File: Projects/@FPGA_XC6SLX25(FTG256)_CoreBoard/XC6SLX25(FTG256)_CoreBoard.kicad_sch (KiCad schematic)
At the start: 155 parts, among them J1 MTA18ASF2G72HZ-2G3A2, U1 XC6SLX25-FTG256, U2 W25Q128JVS, U3 TPS51200DRC, U4 MP214x, U5 MP214x, U6 MP214x, U7 MP214x, X1 ECS-2520MV-xxx-xx

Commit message: XC6SLX25(FTG256)_CoreBoard Checked
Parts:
- added LOGO1: StarsRiver, lib:LOGO_StarsRiver, symbol Mechanical:MountingHole
- added LOGO2: Xilinx, lib:LOGO_Xilinx, symbol Mechanical:MountingHole
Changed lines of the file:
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@@
     (pin "2")
   )
+  (symbol (lib_id "Mechanical:MountingHole") (at 435.61 278.13 0) (unit 1)
+    (in_bom yes) (on_board yes) (fields_autoplaced)
+    (property "Reference" "LOGO2" (id 0) (at 438.15 276.8599 0)
+      (effects (font (size 1.27 1.27)) (justify left))
+    )
+    (property "Value" "Xilinx" (id 1) (at 438.15 279.3999 0)
+      (effects (font (size 1.27 1.27)) (justify left))
+    )
+    (property "Footprint" "lib:LOGO_Xilinx" (id 2) (at 435.61 278.13 0)
+      (effects (font (size 1.27 1.27)) hide)
+    )
+    (property "Datasheet" "~" (id 3) (at 435.61 278.13 0)
+      (effects (font (size 1.27 1.27)) hide)
+    )
+  )
   (symbol (lib_id "Device:C") (at 294.64 45.72 0) (unit 1)
     (in_bom yes) (on_board yes)
@@
     (pin "2")
   )
+  (symbol (lib_id "Mechanical:MountingHole") (at 435.61 270.51 0) (unit 1)
+    (in_bom yes) (on_board yes) (fields_autoplaced)
+    (property "Reference" "LOGO1" (id 0) (at 438.15 269.2399 0)
+      (effects (font (size 1.27 1.27)) (justify left))
+    )
+    (property "Value" "StarsRiver" (id 1) (at 438.15 271.7799 0)
+      (effects (font (size 1.27 1.27)) (justify left))
+    )
+    (property "Footprint" "lib:LOGO_StarsRiver" (id 2) (at 435.61 270.51 0)
+      (effects (font (size 1.27 1.27)) hide)
+    )
+    (property "Datasheet" "~" (id 3) (at 435.61 270.51 0)
+      (effects (font (size 1.27 1.27)) hide)
+    )
+  )
   (symbol (lib_id "power:+2V5") (at 77.47 41.91 0) (unit 1)
     (in_bom yes) (on_board yes) (fields_autoplaced)
@@
       (reference "LED2") (unit 1) (value "LED") (footprint "LED_SMD:LED_0402_1005Metric")
     )
+    (path "/728ba05c-7334-4064-9520-97bdb4f97950"
+      (reference "LOGO1") (unit 1) (value "StarsRiver") (footprint "lib:LOGO_StarsRiver")
+    )
+    (path "/2db6cabb-1ba4-45d2-89d5-34c37407f197"
+      (reference "LOGO2") (unit 1) (value "Xilinx") (footprint "lib:LOGO_Xilinx")
+    )
     (path "/e5f2248d-47e0-4488-b6fe-0d3e6f9140c0"

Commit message: XC6SLX25(FTG256)_CoreBoard increase 3V3,2V5 power output ability
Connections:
- net +2V5: now also J1.77, J1.79
- net +3V3: now also J1.243
- net GND: no longer J1.243, J1.245
- no-connect marks 62 -> 61
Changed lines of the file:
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@@
   (junction (at 118.11 435.61) (diameter 0) (color 0 0 0 0)
   )
+  (junction (at 452.12 109.22) (diameter 0) (color 0 0 0 0)
+  )
   (junction (at 77.47 243.84) (diameter 0) (color 0 0 0 0)
   )
@@
   (junction (at 519.43 411.48) (diameter 0) (color 0 0 0 0)
   )
-  (junction (at 452.12 104.14) (diameter 0) (color 0 0 0 0)
-  )
   (junction (at 688.34 201.93) (diameter 0) (color 0 0 0 0)
   )
@@
   (junction (at 626.11 105.41) (diameter 0) (color 0 0 0 0)
   )
+  (junction (at 486.41 167.64) (diameter 0) (color 0 0 0 0)
+  )
   (junction (at 119.38 243.84) (diameter 0) (color 0 0 0 0)
   )
@@
   (junction (at 322.58 55.88) (diameter 0) (color 0 0 0 0)
   )
+  (junction (at 516.89 167.64) (diameter 0) (color 0 0 0 0)
+  )
   (junction (at 260.35 49.53) (diameter 0) (color 0 0 0 0)
   )
@@
   )
   (no_connect (at 516.89 231.14))
+  (no_connect (at 452.12 104.14))
   (no_connect (at 516.89 198.12))
   (no_connect (at 516.89 208.28))
@@
   (no_connect (at 516.89 162.56))
   (no_connect (at 516.89 165.1))
-  (no_connect (at 516.89 167.64))
-  (no_connect (at 516.89 170.18))
   (no_connect (at 516.89 172.72))
   (no_connect (at 516.89 177.8))
@@
     (stroke (width 0) (type default) (color 0 0 0 0))
   )
+  (wire (pts (xy 452.12 106.68) (xy 452.12 109.22))
+    (stroke (width 0) (type default) (color 0 0 0 0))
+  )
   (wire (pts (xy 314.96 266.7) (xy 314.96 278.13))
     (stroke (width 0) (type default) (color 0 0 0 0))
@@
     (stroke (width 0) (type default) (color 0 0 0 0))
   )
-  (wire (pts (xy 452.12 104.14) (xy 452.12 106.68))
-    (stroke (width 0) (type default) (color 0 0 0 0))
-  )
   (wire (pts (xy 637.54 419.1) (xy 645.16 419.1))
     (stroke (width 0) (type default) (color 0 0 0 0))
@@
     (stroke (width 0) (type default) (color 0 0 0 0))
   )
+  (wire (pts (xy 516.89 167.64) (xy 516.89 170.18))
+    (stroke (width 0) (type default) (color 0 0 0 0))
+  )
   (wire (pts (xy 695.96 411.48) (xy 694.69 411.48))
     (stroke (width 0) (type default) (color 0 0 0 0))
@@
     (stroke (width 0) (type default) (color 0 0 0 0))
   )
+  (wire (pts (xy 486.41 167.64) (xy 486.41 170.18))
+    (stroke (width 0) (type default) (color 0 0 0 0))
+  )
   (wire (pts (xy 53.34 76.2) (xy 49.53 76.2))
     (stroke (width 0) (type default) (color 0 0 0 0))
@@
     (pin "1")
   )
-  (symbol (lib_id "power:+2V5") (at 486.41 170.18 90) (unit 1)
+  (symbol (lib_id "power:+2V5") (at 516.89 167.64 270) (mirror x) (unit 1)
     (in_bom yes) (on_board yes)
-    (property "Reference" "#PWR0199" (id 0) (at 490.22 170.18 0)
+    (property "Reference" "#PWR0199" (id 0) (at 513.08 167.64 0)
       (effects (font (size 1.27 1.27)) hide)
     )
-    (property "Value" "+2V5" (id 1) (at 480.2655 170.18 90))
-    (property "Footprint" "" (id 2) (at 486.41 170.18 0)
+    (property "Value" "+2V5" (id 1) (at 523.0345 167.64 90))
+    (property "Footprint" "" (id 2) (at 516.89 167.64 0)
       (effects (font (size 1.27 1.27)) hide)
     )
-    (property "Datasheet" "" (id 3) (at 486.41 170.18 0)
+    (property "Datasheet" "" (id 3) (at 516.89 167.64 0)
       (effects (font (size 1.27 1.27)) hide)
     )
@@
     (pin "2")
   )
-  (symbol (lib_id "power:GND") (at 452.12 104.14 90) (unit 1)
-    (in_bom yes) (on_board yes)
-    (property "Reference" "#PWR0202" (id 0) (at 458.47 104.14 0)
-      (effects (font (size 1.27 1.27)) hide)
-    )
-    (property "Value" "GND" (id 1) (at 459.105 104.931 90)
-      (effects (font (size 1.27 1.27)) (justify left))
-    )
-    (property "Footprint" "" (id 2) (at 452.12 104.14 0)
-      (effects (font (size 1.27 1.27)) hide)
-    )
-    (property "Datasheet" "" (id 3) (at 452.12 104.14 0)
-      (effects (font (size 1.27 1.27)) hide)
-    )
-    (pin "1")
-  )
   (symbol (lib_id "Device:R_Pack02") (at 676.91 259.08 90) (unit 1)
     (in_bom yes) (on_board yes) (fields_autoplaced)
@@
       (reference "#PWR0201") (unit 1) (value "+3.3V") (footprint "")
     )
-    (path "/9ca88638-10ae-46ec-b089-251fb43b6d5a"
-      (reference "#PWR0202") (unit 1) (value "GND") (footprint "")
-    )
     (path "/130dd5b2-8c41-43dd-a094-4ef11acea7e6"

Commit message: FPGA_XC6SLX25_CoreBoard optimize (FIN)
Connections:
- net DDR_D10: now also RN9.5 (R4.2); no longer RN9.6 (R3.2)
- net DDR_D8: now also RN9.6 (R3.2); no longer RN9.5 (R4.2)
- net DDR_MD8: now also RN9.3 (R3.1); no longer RN9.4 (R4.1)
- net DDR_MD9: now also RN9.4 (R4.1); no longer RN9.3 (R3.1)
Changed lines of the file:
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@@
     (effects (font (size 1.27 1.27)) (justify right bottom))
   )
-  (label "DDR_MD9" (at 645.16 279.4 0)
+  (label "DDR_MD9" (at 645.16 276.86 0)
     (effects (font (size 1.27 1.27)) (justify left bottom))
   )
@@
     (effects (font (size 1.27 1.27)) (justify left bottom))
   )
-  (label "DDR_D8" (at 635 276.86 180)
+  (label "DDR_D8" (at 635 279.4 180)
     (effects (font (size 1.27 1.27)) (justify right bottom))
   )
@@
     (effects (font (size 1.27 1.27)) (justify left bottom))
   )
-  (label "DDR_D10" (at 635 279.4 180)
+  (label "DDR_D10" (at 635 276.86 180)
     (effects (font (size 1.27 1.27)) (justify right bottom))
   )
@@
     (effects (font (size 1.27 1.27)) (justify left bottom))
   )
-  (label "DDR_MD8" (at 645.16 276.86 0)
-    (effects (font (size 1.27 1.27)) (justify left bottom))
-  )
+  (label "DDR_MD8" (at 645.16 279.4 0)
+    (effects (font (size 1.27 1.27)) (justify left bottom))
+  )

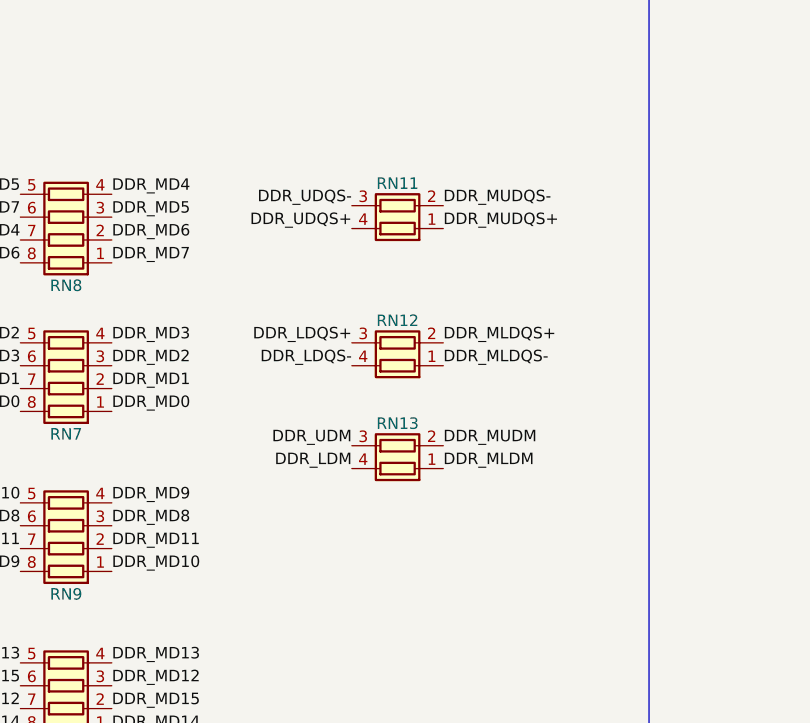
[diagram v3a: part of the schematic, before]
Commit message: replace ArrayResistence(x2) with x4
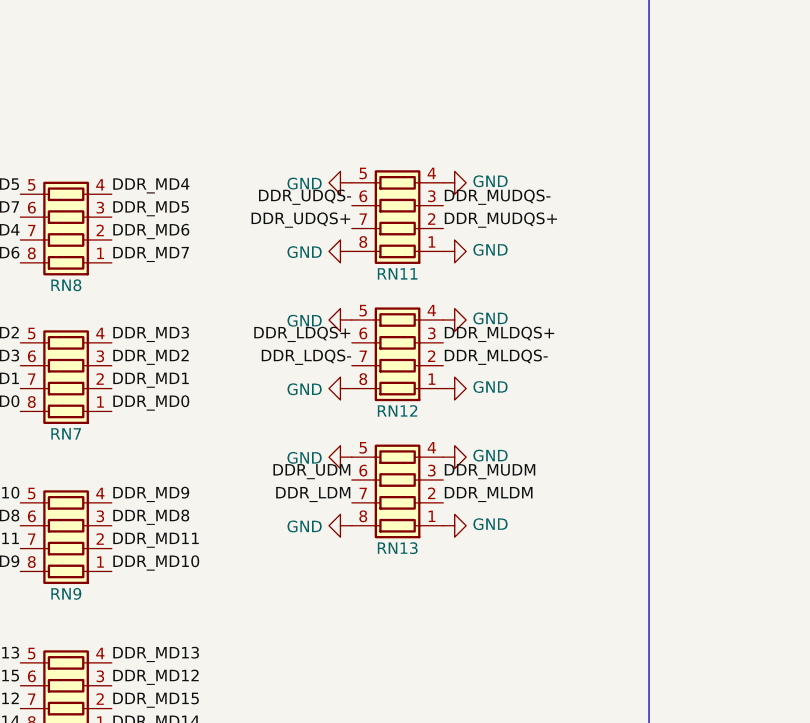
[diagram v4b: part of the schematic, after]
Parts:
- removed RN11, RN12, RN13: R_Pack02, Resistor_SMD:R_Array_Convex_2x0402, symbol Device:R_Pack02
- added RN11, RN12, RN13: R_Pack04, Resistor_SMD:R_Array_Concave_4x0402, symbol Device:R_Pack04
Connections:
- net DDR_LDM: now also RN13.7 (R2.2)
- net DDR_LDQS+: now also RN12.6 (R3.2)
- net DDR_LDQS-: now also RN12.7 (R2.2)
- net DDR_MLDM: now also RN13.2 (R2.1)
- net DDR_MLDQS+: now also RN12.3 (R3.1)
- net DDR_MLDQS-: now also RN12.2 (R2.1)
- net DDR_MUDM: now also RN13.3 (R3.1)
- net DDR_MUDQS+: now also RN11.2 (R2.1)
- net DDR_MUDQS-: now also RN11.3 (R3.1)
- net DDR_UDM: now also RN13.6 (R3.2)
- net DDR_UDQS+: now also RN11.7 (R2.2)
- net DDR_UDQS-: now also RN11.6 (R3.2)
- net GND: now also RN11.1 (R1.1), RN11.4 (R4.1), RN11.5 (R4.2), RN11.8 (R1.2), RN12.1 (R1.1), RN12.4 (R4.1), RN12.5 (R4.2), RN12.8 (R1.2), RN13.1 (R1.1), RN13.4 (R4.1), RN13.5 (R4.2), RN13.8 (R1.2)
